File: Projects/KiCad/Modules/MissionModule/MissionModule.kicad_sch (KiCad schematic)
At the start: 50 parts, among them J1 Conn_01x08, J2 Micro_SD_Card_Det_Hirose_DM3AT, SW1 SW_DIP_x02, U1 MCP2562-E-P, U2 MCP2515-I/P, U3 NJM7805SDL1, U5 TLP222A, U6 ABX00012, U7 MB85RS2MT, U8 MB85RS2MT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

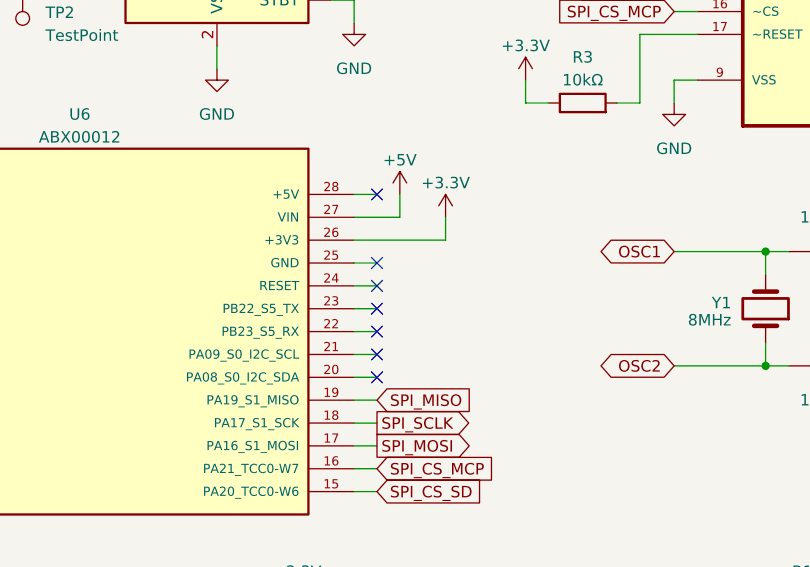
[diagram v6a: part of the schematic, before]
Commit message: 配線の繋ぎ忘れを修正
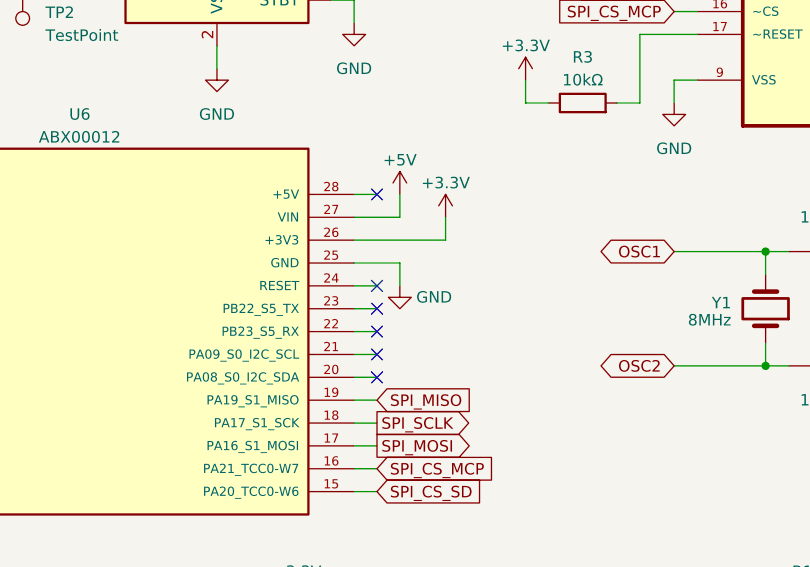
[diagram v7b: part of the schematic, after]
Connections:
- net GND: now also U6.25 (GND)
- no-connect marks 20 -> 19
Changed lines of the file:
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@@
   (junction (at 248.92 102.87) (diameter 0) (color 0 0 0 0)
   )
-  (no_connect (at 110.49 83.82))
   (no_connect (at 199.39 40.64))
   (no_connect (at 110.49 93.98))
@@
     (stroke (width 0) (type default))
   )
-  (wire (pts (xy 107.95 83.82) (xy 110.49 83.82))
+  (wire (pts (xy 107.95 83.82) (xy 113.03 83.82))
     (stroke (width 0) (type default))
   )
@@
   )
   (wire (pts (xy 72.39 189.23) (xy 74.93 189.23))
+    (stroke (width 0) (type default))
+  )
+  (wire (pts (xy 113.03 83.82) (xy 113.03 86.36))
     (stroke (width 0) (type default))
   )
@@
         )
       )
+    )
+  )
+  (symbol (lib_id "power:GND") (at 113.03 86.36 0) (unit 1)
+    (in_bom yes) (on_board yes) (dnp no)
+    (property "Reference" "#PWR02" (at 113.03 92.71 0)
+      (effects (font (size 1.27 1.27)) hide)
+    )
+    (property "Value" "GND" (at 116.84 87.63 0)
+      (effects (font (size 1.27 1.27)))
+    )
+    (property "Footprint" "" (at 113.03 86.36 0)
+      (effects (font (size 1.27 1.27)) hide)
+    )
+    (property "Datasheet" "" (at 113.03 86.36 0)
+      (effects (font (size 1.27 1.27)) hide)
+    )
+    (pin "1")
+    (instances
+      (project "MissionModule"
+        (path "/ea1ed597-7cd3-4340-902e-bdce8f2d7a62"
+          (reference "#PWR02") (unit 1)
+        )
+      )

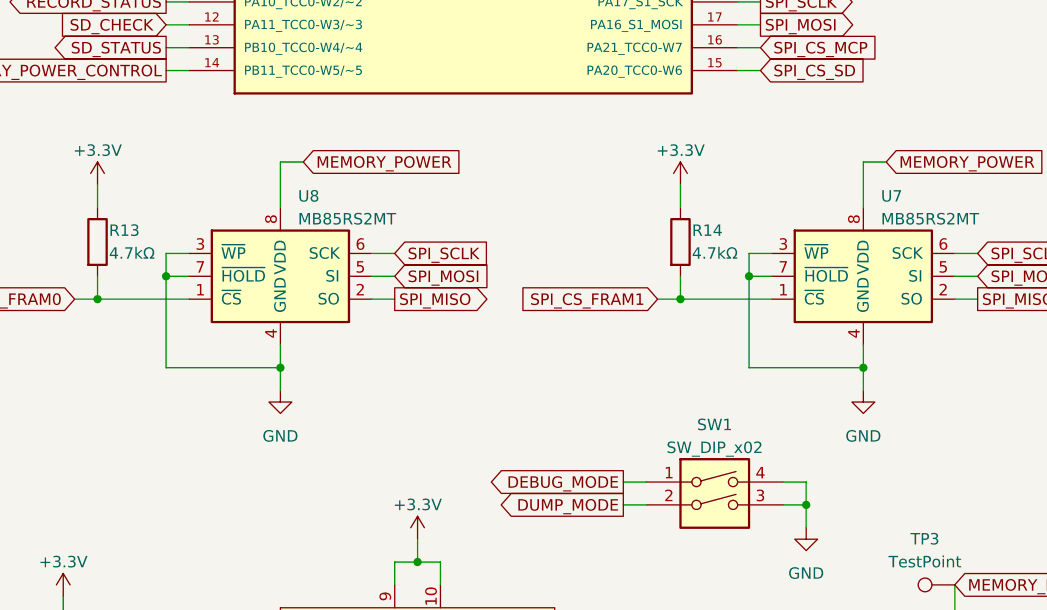
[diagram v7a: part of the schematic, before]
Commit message: FRAMのWPとHOLDをHIGHに固定
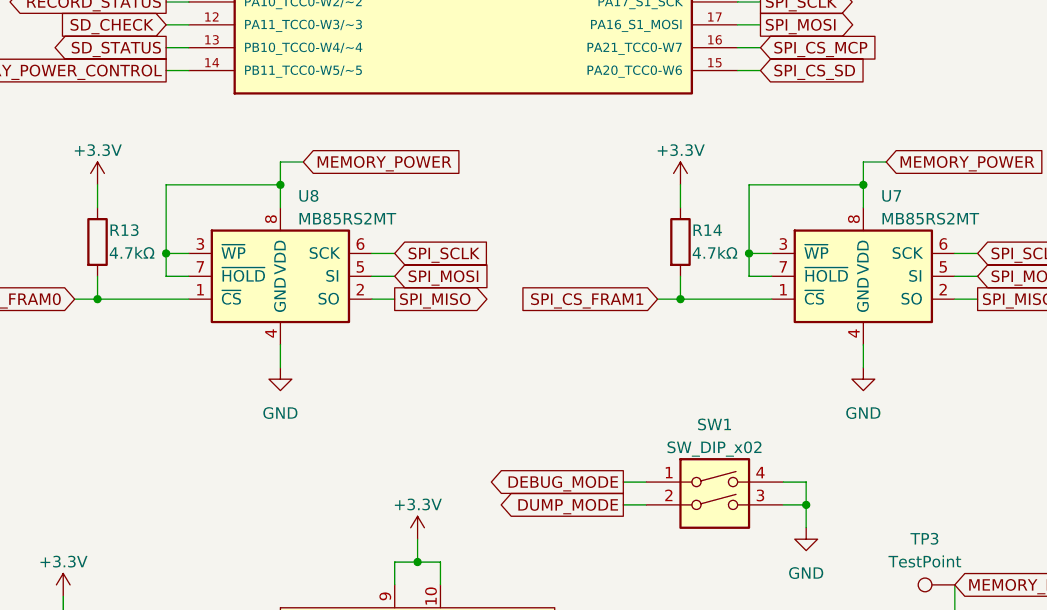
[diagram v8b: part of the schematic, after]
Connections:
- net GND: no longer U7.3 (~{WP}), U7.7 (~{HOLD}), U8.3 (~{WP}), U8.7 (~{HOLD})
- net MEMORY_POWER: now also U7.3 (~{WP}), U7.7 (~{HOLD}), U8.3 (~{WP}), U8.7 (~{HOLD})
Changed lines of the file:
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@@
 (kicad_sch (version 20230121) (generator eeschema)
   (paper "A4")
+  (junction (at 121.92 121.92) (diameter 0) (color 0 0 0 0)
+  )
   (junction (at 236.22 115.57) (diameter 0) (color 0 0 0 0)
   )
@@
   (junction (at 25.4 30.48) (diameter 0) (color 0 0 0 0)
   )
+  (junction (at 57.15 121.92) (diameter 0) (color 0 0 0 0)
+  )
   (junction (at 25.4 25.4) (diameter 0) (color 0 0 0 0)
   )
@@
   (junction (at 223.52 102.87) (diameter 0) (color 0 0 0 0)
   )
+  (junction (at 109.22 129.54) (diameter 0) (color 0 0 0 0)
+  )
   (junction (at 119.38 177.8) (diameter 0) (color 0 0 0 0)
   )
@@
   (junction (at 36.83 134.62) (diameter 0) (color 0 0 0 0)
   )
-  (junction (at 44.45 132.08) (diameter 0) (color 0 0 0 0)
-  )
-  (junction (at 57.15 142.24) (diameter 0) (color 0 0 0 0)
-  )
   (junction (at 71.12 45.72) (diameter 0) (color 0 0 0 0)
   )
-  (junction (at 109.22 132.08) (diameter 0) (color 0 0 0 0)
-  )
   (junction (at 72.39 189.23) (diameter 0) (color 0 0 0 0)
   )
+  (junction (at 44.45 129.54) (diameter 0) (color 0 0 0 0)
+  )
   (junction (at 166.37 95.25) (diameter 0) (color 0 0 0 0)
-  )
-  (junction (at 121.92 142.24) (diameter 0) (color 0 0 0 0)
   )
   (junction (at 223.52 92.71) (diameter 0) (color 0 0 0 0)
@@
     (stroke (width 0) (type default))
   )
+  (wire (pts (xy 109.22 121.92) (xy 109.22 129.54))
+    (stroke (width 0) (type default))
+  )
   (wire (pts (xy 196.85 30.48) (xy 199.39 30.48))
     (stroke (width 0) (type default))
@@
     (stroke (width 0) (type default))
   )
+  (wire (pts (xy 57.15 121.92) (xy 57.15 124.46))
+    (stroke (width 0) (type default))
+  )
   (wire (pts (xy 146.05 58.42) (xy 139.7 58.42))
     (stroke (width 0) (type default))
@@
     (stroke (width 0) (type default))
   )
+  (wire (pts (xy 121.92 121.92) (xy 109.22 121.92))
+    (stroke (width 0) (type default))
+  )
   (wire (pts (xy 95.25 154.94) (xy 97.79 154.94))
     (stroke (width 0) (type default))
@@
     (stroke (width 0) (type default))
   )
-  (wire (pts (xy 57.15 119.38) (xy 57.15 124.46))
-    (stroke (width 0) (type default))
-  )
   (wire (pts (xy 167.64 140.97) (xy 170.18 140.97))
     (stroke (width 0) (type default))
@@
     (stroke (width 0) (type default))
   )
+  (wire (pts (xy 57.15 119.38) (xy 57.15 121.92))
+    (stroke (width 0) (type default))
+  )
   (wire (pts (xy 240.03 92.71) (xy 248.92 92.71))
     (stroke (width 0) (type default))
@@
     (stroke (width 0) (type default))
   )
+  (wire (pts (xy 25.4 36.83) (xy 24.13 36.83))
+    (stroke (width 0) (type default))
+  )
+  (wire (pts (xy 77.47 46.99) (xy 77.47 45.72))
+    (stroke (width 0) (type default))
+  )
+  (wire (pts (xy 33.02 177.8) (xy 33.02 180.34))
+    (stroke (width 0) (type default))
+  )
+  (wire (pts (xy 44.45 81.28) (xy 46.99 81.28))
+    (stroke (width 0) (type default))
+  )
+  (wire (pts (xy 252.73 60.96) (xy 252.73 63.5))
+    (stroke (width 0) (type default))
+  )
+  (bus (pts (xy 38.1 43.18) (xy 38.1 55.88))
+    (stroke (width 0) (type default))
+  )
+  (wire (pts (xy 25.4 35.56) (xy 35.56 35.56))
+    (stroke (width 0) (type default))
+  )
   (wire (pts (xy 121.92 139.7) (xy 121.92 142.24))
     (stroke (width 0) (type default))
   )
-  (wire (pts (xy 25.4 36.83) (xy 24.13 36.83))
-    (stroke (width 0) (type default))
-  )
-  (wire (pts (xy 77.47 46.99) (xy 77.47 45.72))
-    (stroke (width 0) (type default))
-  )
-  (wire (pts (xy 33.02 177.8) (xy 33.02 180.34))
-    (stroke (width 0) (type default))
-  )
-  (wire (pts (xy 44.45 81.28) (xy 46.99 81.28))
-    (stroke (width 0) (type default))
-  )
-  (wire (pts (xy 252.73 60.96) (xy 252.73 63.5))
-    (stroke (width 0) (type default))
-  )
-  (bus (pts (xy 38.1 43.18) (xy 38.1 55.88))
-    (stroke (width 0) (type default))
-  )
-  (wire (pts (xy 25.4 35.56) (xy 35.56 35.56))
-    (stroke (width 0) (type default))
-  )
-  (wire (pts (xy 121.92 142.24) (xy 121.92 144.78))
-    (stroke (width 0) (type default))
-  )
   (wire (pts (xy 111.76 129.54) (xy 109.22 129.54))
     (stroke (width 0) (type default))
@@
     (stroke (width 0) (type default))
   )
+  (wire (pts (xy 44.45 121.92) (xy 57.15 121.92))
+    (stroke (width 0) (type default))
+  )
   (wire (pts (xy 222.25 50.8) (xy 222.25 53.34))
     (stroke (width 0) (type default))
@@
     (stroke (width 0) (type default))
   )
-  (wire (pts (xy 57.15 142.24) (xy 57.15 144.78))
-    (stroke (width 0) (type default))
-  )
   (wire (pts (xy 24.13 29.21) (xy 25.4 29.21))
     (stroke (width 0) (type default))
@@
     (stroke (width 0) (type default))
   )
-  (wire (pts (xy 44.45 132.08) (xy 44.45 142.24))
-    (stroke (width 0) (type default))
-  )
-  (wire (pts (xy 109.22 142.24) (xy 121.92 142.24))
-    (stroke (width 0) (type default))
-  )
   (wire (pts (xy 119.38 177.8) (xy 121.92 177.8))
     (stroke (width 0) (type default))
   )
-  (wire (pts (xy 121.92 119.38) (xy 121.92 124.46))
+  (wire (pts (xy 121.92 119.38) (xy 121.92 121.92))
     (stroke (width 0) (type default))
   )
@@
     (stroke (width 0) (type default))
   )
-  (wire (pts (xy 44.45 142.24) (xy 57.15 142.24))
-    (stroke (width 0) (type default))
-  )
   (wire (pts (xy 161.29 113.03) (xy 161.29 115.57))
     (stroke (width 0) (type default))
@@
     (stroke (width 0) (type default))
   )
-  (wire (pts (xy 109.22 132.08) (xy 109.22 142.24))
-    (stroke (width 0) (type default))
-  )
   (wire (pts (xy 52.07 50.8) (xy 52.07 53.34))
     (stroke (width 0) (type default))
@@
     (stroke (width 0) (type default))
   )
+  (wire (pts (xy 44.45 129.54) (xy 44.45 121.92))
+    (stroke (width 0) (type default))
+  )
   (wire (pts (xy 34.29 134.62) (xy 36.83 134.62))
     (stroke (width 0) (type default))
@@
   )
   (wire (pts (xy 107.95 101.6) (xy 110.49 101.6))
+    (stroke (width 0) (type default))
+  )
+  (wire (pts (xy 121.92 121.92) (xy 121.92 124.46))
     (stroke (width 0) (type default))
   )
@@
     )
   )
-  (symbol (lib_id "power:GND") (at 121.92 144.78 0) (unit 1)
-    (in_bom yes) (on_board yes) (dnp no) (fields_autoplaced)
-    (property "Reference" "#PWR037" (at 121.92 151.13 0)
-      (effects (font (size 1.27 1.27)) hide)
-    )
-    (property "Value" "GND" (at 121.92 149.86 0)
-      (effects (font (size 1.27 1.27)))
-    )
-    (property "Footprint" "" (at 121.92 144.78 0)
-      (effects (font (size 1.27 1.27)) hide)
-    )
-    (property "Datasheet" "" (at 121.92 144.78 0)
+  (symbol (lib_id "power:GND") (at 121.92 142.24 0) (unit 1)
+    (in_bom yes) (on_board yes) (dnp no) (fields_autoplaced)
+    (property "Reference" "#PWR037" (at 121.92 148.59 0)
+      (effects (font (size 1.27 1.27)) hide)
+    )
+    (property "Value" "GND" (at 121.92 147.32 0)
+      (effects (font (size 1.27 1.27)))
+    )
+    (property "Footprint" "" (at 121.92 142.24 0)
+      (effects (font (size 1.27 1.27)) hide)
+    )
+    (property "Datasheet" "" (at 121.92 142.24 0)
       (effects (font (size 1.27 1.27)) hide)
     )
@@
     )
   )
-  (symbol (lib_id "power:GND") (at 57.15 144.78 0) (unit 1)
-    (in_bom yes) (on_board yes) (dnp no) (fields_autoplaced)
-    (property "Reference" "#PWR038" (at 57.15 151.13 0)
-      (effects (font (size 1.27 1.27)) hide)
-    )
-    (property "Value" "GND" (at 57.15 149.86 0)
-      (effects (font (size 1.27 1.27)))
-    )
-    (property "Footprint" "" (at 57.15 144.78 0)
-      (effects (font (size 1.27 1.27)) hide)
-    )
-    (property "Datasheet" "" (at 57.15 144.78 0)
-      (effects (font (size 1.27 1.27)) hide)
-    )
+  (symbol (lib_id "power:GND") (at 57.15 142.24 0) (unit 1)
+    (in_bom yes) (on_board yes) (dnp no) (fields_autoplaced)
+    (property "Reference" "#PWR038" (at 57.15 148.59 0)
+      (effects (font (size 1.27 1.27)) hide)
+    )
+    (property "Value" "GND" (at 57.15 147.32 0)
+      (effects (font (size 1.27 1.27)))
+    )
+    (property "Footprint" "" (at 57.15 142.24 0)
+      (effects (font (size 1.27 1.27)) hide)
+    )
+    (property "Datasheet" "" (at 57.15 142.24 0)
+      (effects (font (size 1.27 1.27)) hide)
+    )
